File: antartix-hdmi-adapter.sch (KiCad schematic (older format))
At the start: 46 parts, among them IC2 TPD8S009DSMR, J10 3-794680-8, J11 1-794610-1, J12 1-794610-1, J13 1-794610-1, J14 1-794610-1, J16 1-794610-1, J17 1-794610-1, J18 1-794610-1, J19 1-794610-1, J7 QTE-020-04-L-D-A, J8 WE_629105150521, J9 WE_685119136923, Q1 FDC6330L, Q2 FDC6330L, Q3 FDC6330L, U7 FT230XS-R

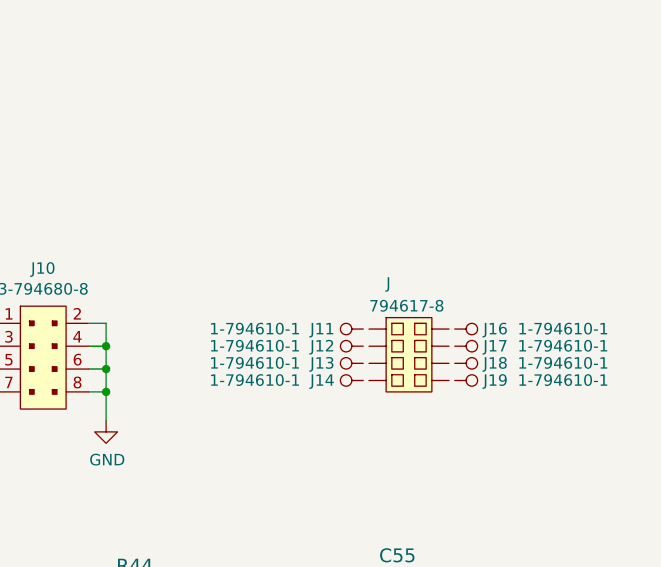
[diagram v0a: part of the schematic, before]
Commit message: Update libraries fields
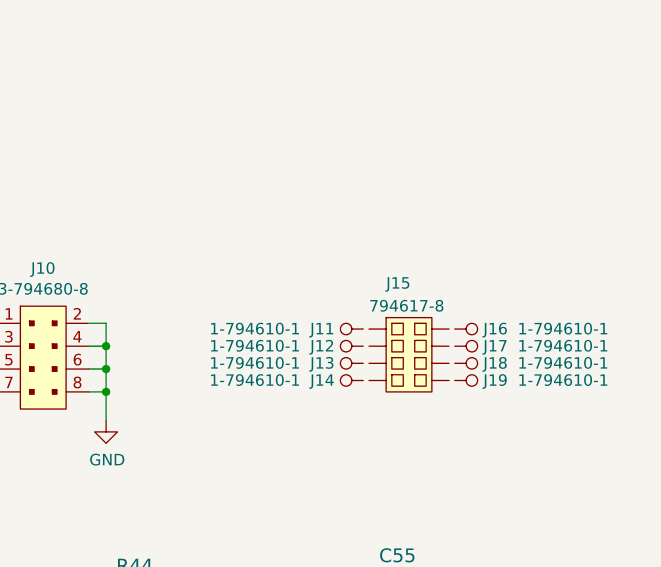
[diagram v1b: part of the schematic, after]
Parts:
- renumbered J to J15
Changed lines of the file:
@@
 $EndComp
 $Comp
-L antartix-arty-controller:794617-8 J
+L antartix-arty-controller:794617-8 J15
 U 1 1 60664A1A
 P 14750 4525
-F 0 "J" H 14650 4925 50  0000 L CNN
+F 0 "J15" H 14650 4925 50  0000 L CNN
 F 1 "794617-8" H 14575 4825 50  0000 L CNN
 F 2 "antartix-arty-controller-footprints:3-794617-8" H 14950 4725 60  0001 L CNN

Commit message: Update naming convention
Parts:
- C49, C50, C53: footprint antartix-arty-controller-footprints:0402-cap -> scalenode-adapter-footprints:0402-cap; symbol antartix-arty-controller:C_100n_0402 -> scalenode-adapter:C_100n_0402
- C51, C52: footprint antartix-arty-controller-footprints:0402-cap -> scalenode-adapter-footprints:0402-cap; symbol antartix-arty-controller:C_1u_0402 -> scalenode-adapter:C_1u_0402
- C54: footprint antartix-arty-controller-footprints:0603-cap -> scalenode-adapter-footprints:0603-cap; symbol antartix-arty-controller:C_22u_0603 -> scalenode-adapter:C_22u_0603
- C55, C56, C57: footprint antartix-arty-controller-footprints:0402-cap -> scalenode-adapter-footprints:0402-cap; symbol antartix-arty-controller:C_470p_0402 -> scalenode-adapter:C_470p_0402
- D10: footprint antartix-arty-controller-footprints:SOT-3 -> scalenode-adapter-footprints:SOT-3; symbol antartix-arty-controller:TPD2E009 -> scalenode-adapter:TPD2E009
- D8, D9: footprint antartix-arty-controller-footprints:LED_0603 -> scalenode-adapter-footprints:LED_0603; symbol antartix-arty-controller:LG_L29K-G2J1-24-Z -> scalenode-adapter:LG_L29K-G2J1-24-Z
- FB2: footprint antartix-arty-controller-footprints:0805-res -> scalenode-adapter-footprints:0805-res; symbol antartix-arty-controller:BLM21SP111BH1 -> scalenode-adapter:BLM21SP111BH1
- IC2: footprint antartix-arty-controller-footprints:R-PDSO-N15 -> scalenode-adapter-footprints:R-PDSO-N15; symbol antartix-arty-controller:TPD8S009DSMR -> scalenode-adapter:TPD8S009DSMR
- J10: footprint antartix-arty-controller-footprints:3-794680-8 -> scalenode-adapter-footprints:3-794680-8; symbol antartix-arty-controller:3-794680-8 -> scalenode-adapter:3-794680-8
- J11, J12, J13, J14, J16, J17, J18, J19: footprint antartix-arty-controller-footprints:1-794610-1 -> scalenode-adapter-footprints:1-794610-1; symbol antartix-arty-controller:1-794610-1 -> scalenode-adapter:1-794610-1
- J15: footprint antartix-arty-controller-footprints:3-794617-8 -> scalenode-adapter-footprints:3-794617-8; symbol antartix-arty-controller:794617-8 -> scalenode-adapter:794617-8
- J7: footprint antartix-arty-controller-footprints:QTE-020-04-L-D-A -> scalenode-adapter-footprints:QTE-020-04-L-D-A; symbol antartix-arty-controller:QTE-020-04-L-D-A -> scalenode-adapter:QTE-020-04-L-D-A
- J8: footprint antartix-arty-controller-footprints:USB_Micro_B_Female_629105150521 -> scalenode-adapter-footprints:USB_Micro_B_Female_629105150521; symbol antartix-arty-controller:WE_629105150521 -> scalenode-adapter:WE_629105150521
- J9: footprint antartix-arty-controller-footprints:WE_685119136923 -> scalenode-adapter-footprints:WE_685119136923; symbol antartix-arty-controller:WE_685119136923 -> scalenode-adapter:WE_685119136923
- Q1, Q2, Q3: footprint antartix-arty-controller-footprints:FDC6330L -> scalenode-adapter-footprints:FDC6330L; symbol antartix-arty-controller:FDC6330L -> scalenode-adapter:FDC6330L
- R37: footprint antartix-arty-controller-footprints:0805-res -> scalenode-adapter-footprints:0805-res; symbol antartix-arty-controller:R_0R_0805 -> scalenode-adapter:R_0R_0805
- R38, R39: footprint antartix-arty-controller-footprints:0402-res -> scalenode-adapter-footprints:0402-res; symbol antartix-arty-controller:R_470R_0402 -> scalenode-adapter:R_470R_0402
- R40: footprint antartix-arty-controller-footprints:0402-res -> scalenode-adapter-footprints:0402-res; symbol antartix-arty-controller:R_4k7_0402 -> scalenode-adapter:R_4k7_0402
- R41: footprint antartix-arty-controller-footprints:0402-res -> scalenode-adapter-footprints:0402-res; symbol antartix-arty-controller:R_10k_0402 -> scalenode-adapter:R_10k_0402
- R42, R43: footprint antartix-arty-controller-footprints:0402-res -> scalenode-adapter-footprints:0402-res; symbol antartix-arty-controller:R_0R_0402 -> scalenode-adapter:R_0R_0402
- R44, R45, R46: footprint antartix-arty-controller-footprints:0402-res -> scalenode-adapter-footprints:0402-res; symbol antartix-arty-controller:R_47k_0402 -> scalenode-adapter:R_47k_0402
- R47, R48, R49: footprint antartix-arty-controller-footprints:0402-res -> scalenode-adapter-footprints:0402-res; symbol antartix-arty-controller:R_1k_0402 -> scalenode-adapter:R_1k_0402
- R54, R55: footprint antartix-arty-controller-footprints:0402-res -> scalenode-adapter-footprints:0402-res; symbol antartix-arty-controller:R_22R_0402 -> scalenode-adapter:R_22R_0402
- U7: footprint antartix-arty-controller-footprints:SSOP-16_W3.90mm -> scalenode-adapter-footprints:SSOP-16_W3.90mm; symbol antartix-arty-controller:FT230XS-R -> scalenode-adapter:FT230XS-R
